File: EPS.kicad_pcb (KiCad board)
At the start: 2 copper layers, 35 parts, among them J1 Conn_01x07_Male, J2 Conn_01x03_Male, J3 Conn_01x03_Male, J4 Screw_Terminal_01x02, J5 Screw_Terminal_01x02, U1 AD5245, U2 LM2936-3.3, U3 LT8611

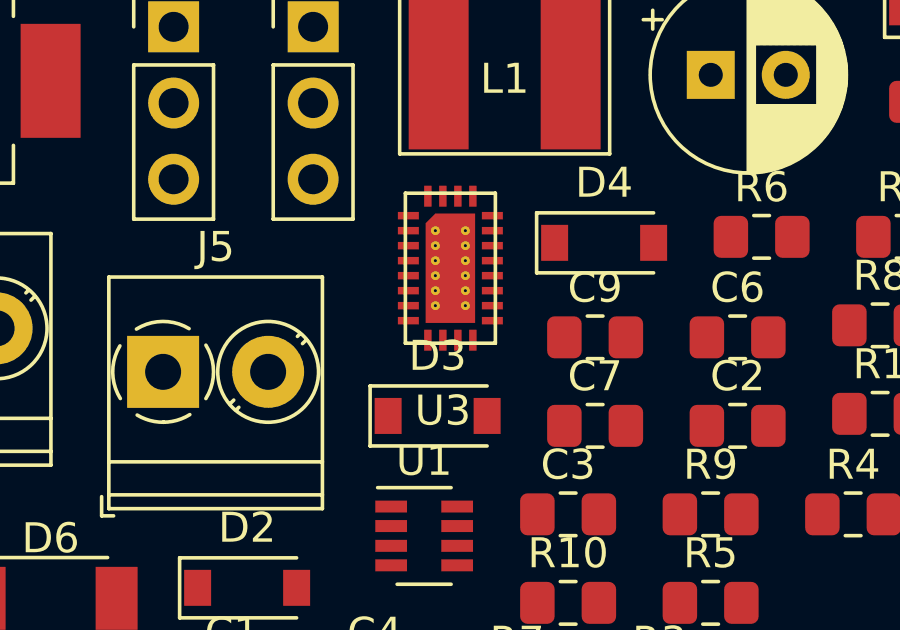
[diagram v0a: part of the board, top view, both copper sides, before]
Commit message: Modified schematic to pass electrical rules check
Added power flags. Resolved error due to stacked power output pins
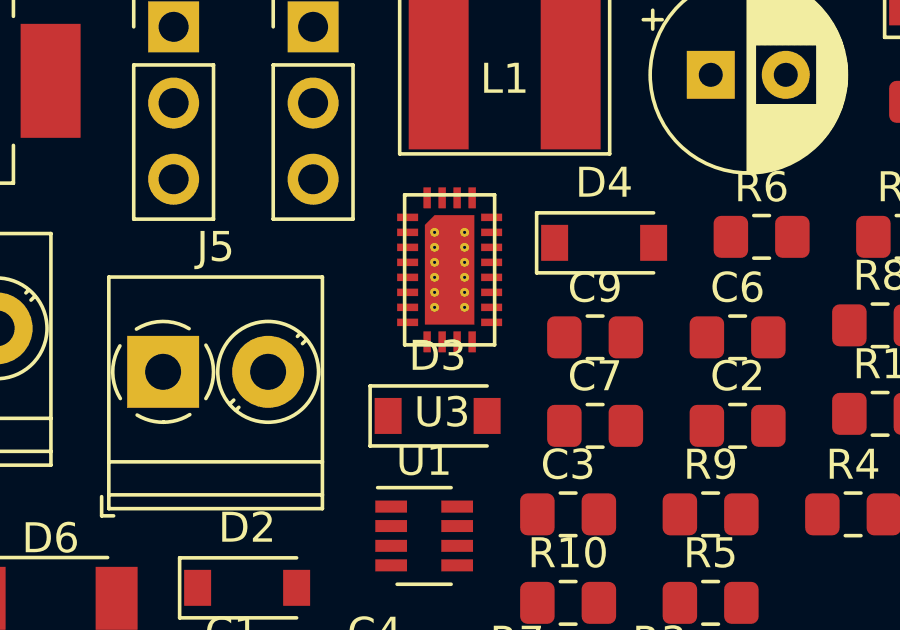
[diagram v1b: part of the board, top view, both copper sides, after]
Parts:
- moved U3 0.06 mm to (151.0, 98.8)
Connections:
- C3 pad 1: Net-(C3-Pad1) -> /INTVCC
- J3 pad 3: (no net) -> /INTVCC
- U3 pad 17: Net-(C3-Pad1) -> /INTVCC

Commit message: PCB Board Layout Created
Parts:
- added ?: , , F.Cu at (159.5, 82.0)
- added REF**: MountingHole_2.5mm, MountingHole:MountingHole_2.5mm, F.Cu at (150.4, 86.1)
- added REF**: MountingHole_2.5mm, MountingHole:MountingHole_2.5mm, F.Cu at (151.3, 40.1)
- added REF**: MountingHole_2.5mm, MountingHole:MountingHole_2.5mm, F.Cu at (111.8, 86.4)
- added REF**: MountingHole_2.5mm, MountingHole:MountingHole_2.5mm, F.Cu at (111.9, 40.5)
- moved C2 67.9 mm to (117.8, 51.2), turned to 270 degrees
- moved R3 62.0 mm to (127.7, 58.8), turned to 180 degrees
- moved D5 61.5 mm to (131.2, 52.0)
- moved R7 61.3 mm to (143.8, 52.2), turned to 90 degrees
- moved C4 60.5 mm to (147.2, 52.0)
- moved R5 60.5 mm to (131.7, 56.2), turned to 90 degrees
- moved R4 58.4 mm to (127.8, 61.5)
- moved R1 57.0 mm to (119.2, 70.0), turned to 90 degrees
- moved R9 55.1 mm to (151.2, 52.5), turned to 90 degrees
- moved U1 54.5 mm to (123.4, 60.2)
- moved C3 53.4 mm to (140.5, 55.5)
- moved R6 53.4 mm to (127.7, 56.2)
- moved J4 52.9 mm to (135.8, 47.9)
- moved R10 52.7 mm to (151.2, 57.2), turned to 90 degrees
- moved R2 52.5 mm to (119.0, 74.5), turned to 270 degrees
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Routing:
- net GND: track 0.00 -> 140.1 mm, vias 0 -> 8
- net /VPAN: track 0.00 -> 92.5 mm
- net +VDC: track 0.00 -> 71.0 mm, vias 0 -> 3
- net Net-(C7-Pad2): track 0.00 -> 55.8 mm, vias 0 -> 3
- net /SYNC: track 0.00 -> 49.5 mm, vias 0 -> 3
- net /PG: track 0.00 -> 46.6 mm, vias 0 -> 2
- net /VDD: track 0.00 -> 29.7 mm
- net /IMON: track 0.00 -> 29.3 mm, vias 0 -> 1
- net Net-(C8-Pad1): track 0.00 -> 26.1 mm, vias 0 -> 3
- net /SCL: track 0.00 -> 23.6 mm, vias 0 -> 2
- net /EXTVIN: track 0.00 -> 21.3 mm
- net Net-(C7-Pad1): track 0.00 -> 21.2 mm
- net /INTVCC: track 0.00 -> 20.4 mm, vias 0 -> 1
- net /SDA: track 0.00 -> 19.7 mm, vias 0 -> 2
- net Net-(D1-Pad2): track 0.00 -> 15.2 mm
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- added copper zone on B.Cu, net +VDC
- added copper zone on F.Cu, net +VDC
- added copper zone on B.Cu, net GND
- added copper zone on F.Cu, net Net-(C6-Pad1)
- added copper zone on F.Cu, net Net-(C7-Pad1)
- added copper zone on F.Cu, net Net-(C7-Pad2)
- added copper zone on F.Cu, net Net-(D6-Pad1)
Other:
- board outline added: 47 x 53 mm
- rule trace_min: 0.2 -> 0.127
- rule via_min_drill: 0.3 -> 0.2
- rule via_min_size: 0.4 -> 0.45

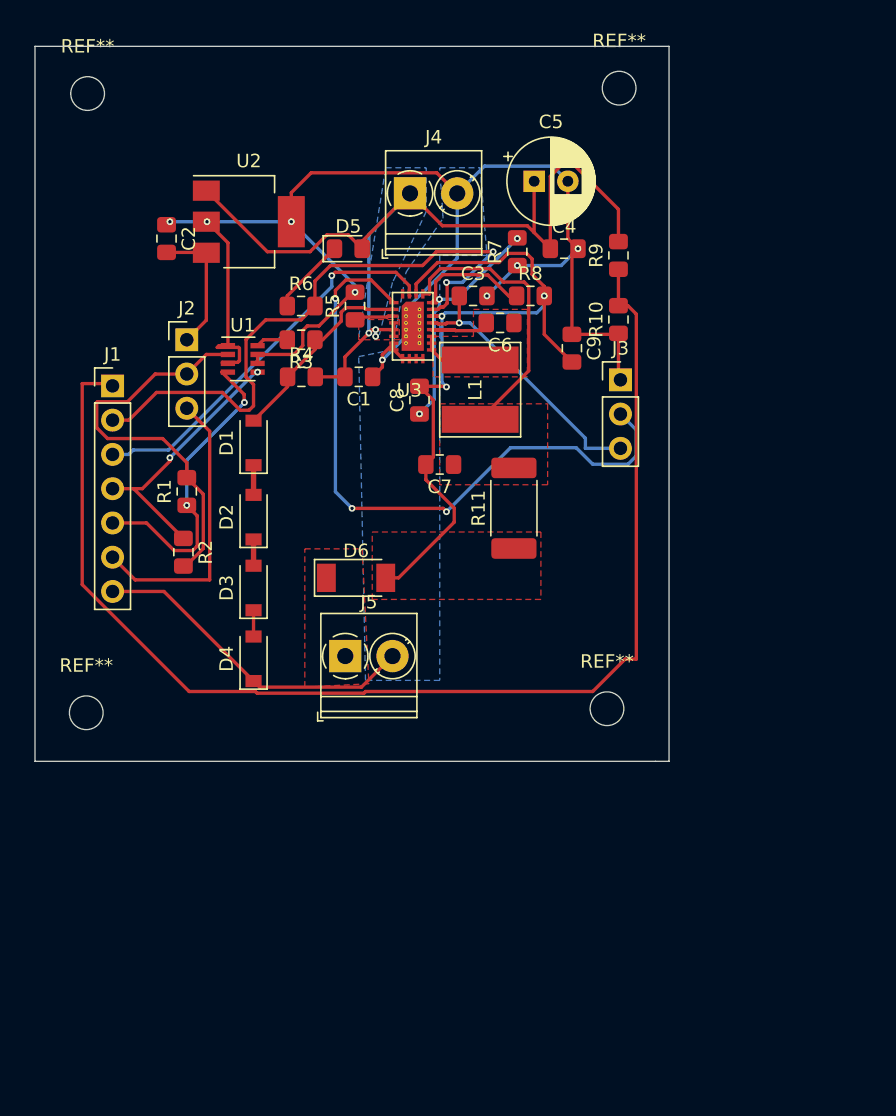
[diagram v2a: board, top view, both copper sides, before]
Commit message: Tweaked polygons and silkscreen
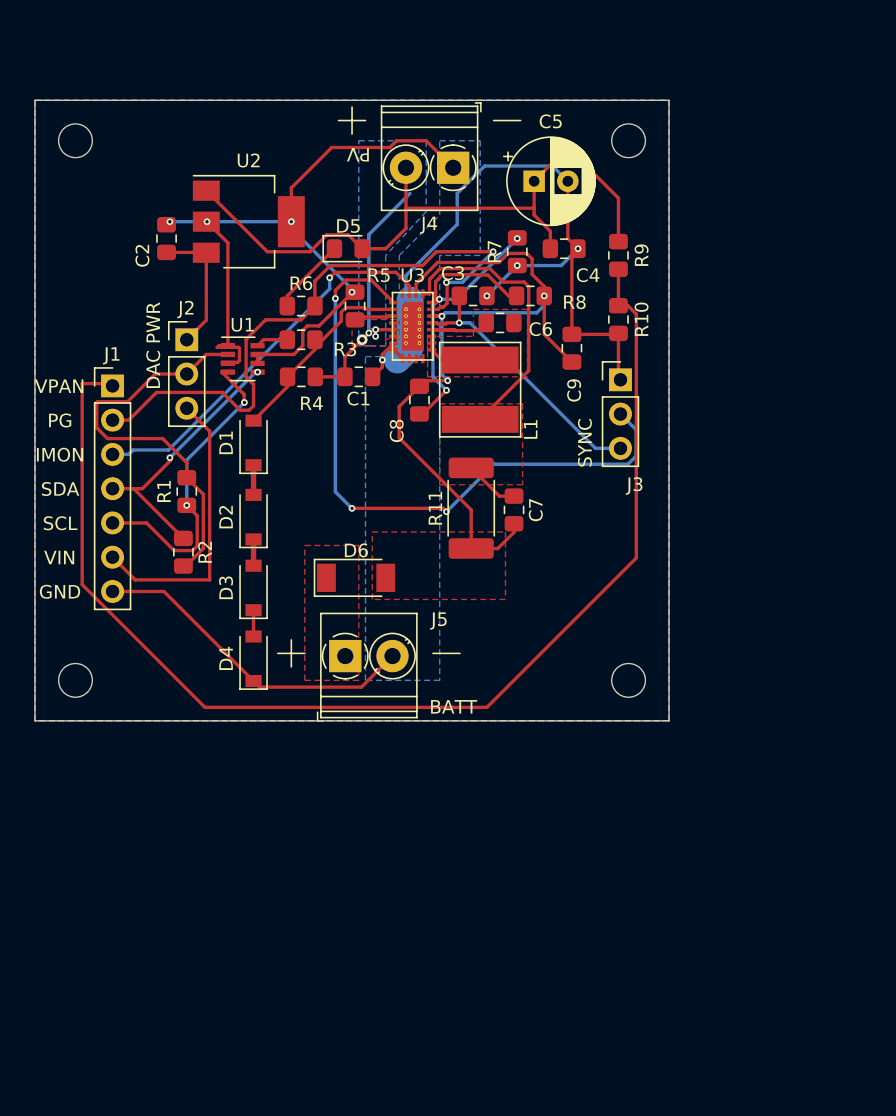
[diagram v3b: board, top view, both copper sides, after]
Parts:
- removed the REF** at (150.4, 86.1)
- removed the REF** at (151.3, 40.1)
- removed the REF** at (111.8, 86.4)
- removed the REF** at (111.9, 40.5)
- added REF**: MountingHole_2.5mm, MountingHole:MountingHole_2.5mm, F.Cu at (152.0, 84.0)
- added REF**: MountingHole_2.5mm, MountingHole:MountingHole_2.5mm, F.Cu at (152.0, 44.0)
- added REF**: MountingHole_2.5mm, MountingHole:MountingHole_2.5mm, F.Cu at (111.0, 84.0)
- added REF**: MountingHole_2.5mm, MountingHole:MountingHole_2.5mm, F.Cu at (111.0, 44.0)
- moved C7 6.46 mm to (143.5, 71.4), turned to 270 degrees
- moved J4 3.72 mm to (139.0, 46.0), turned to 180 degrees
- moved R11 3.16 mm to (140.3, 71.2)
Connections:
- J4 pad 1: +VDC -> GND
- J4 pad 2: GND -> +VDC
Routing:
- net GND: track 140.1 -> 147.4 mm
- net Net-(C7-Pad1): track 21.2 -> 25.3 mm
- net /VPAN: track 92.5 -> 89.0 mm
- net +VDC: track 71.0 -> 69.7 mm, vias 3 -> 4
- net /SYNC: track 49.5 -> 48.5 mm
- net Net-(C8-Pad1): track 26.1 -> 27.1 mm
- net Net-(C7-Pad2): track 55.8 -> 56.4 mm
- added copper zone on F.Cu, net GND
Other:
- board size 47 x 53 mm -> 47 x 46 mm
- board text added: "BATT"
- board text added: "DAC PWR"
- board text added: "GND"
- board text added: "IMON"
- board text added: "MPPT Evaluation Battery Charger Husky Satellite Lab 2020 Designed By Katharine Lundblad"
- board text added: "PG"
- board text added: "PV"
- board text added: "SCL"
- board text added: "SDA"
- board text added: "SYNC"
- board text added: "VIN"
- board text added: "VPAN"
